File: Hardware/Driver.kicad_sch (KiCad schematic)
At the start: 6 parts, among them Q1 MOSFET_CONTACTOR, Q2 MOSFET_PRECHARGE

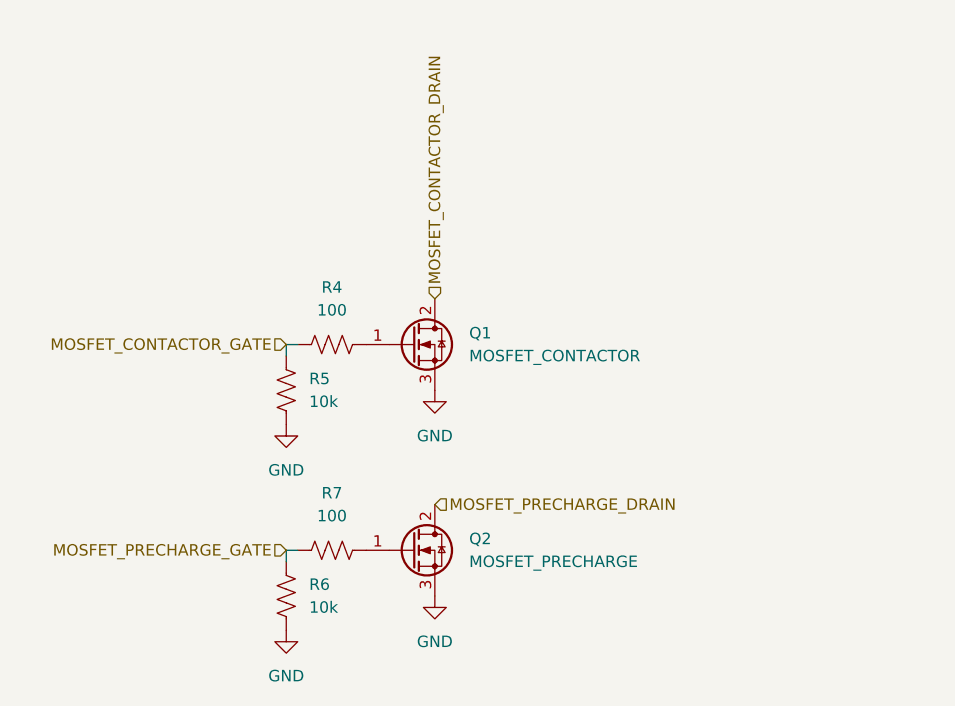
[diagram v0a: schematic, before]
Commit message: Restructure VCU schema
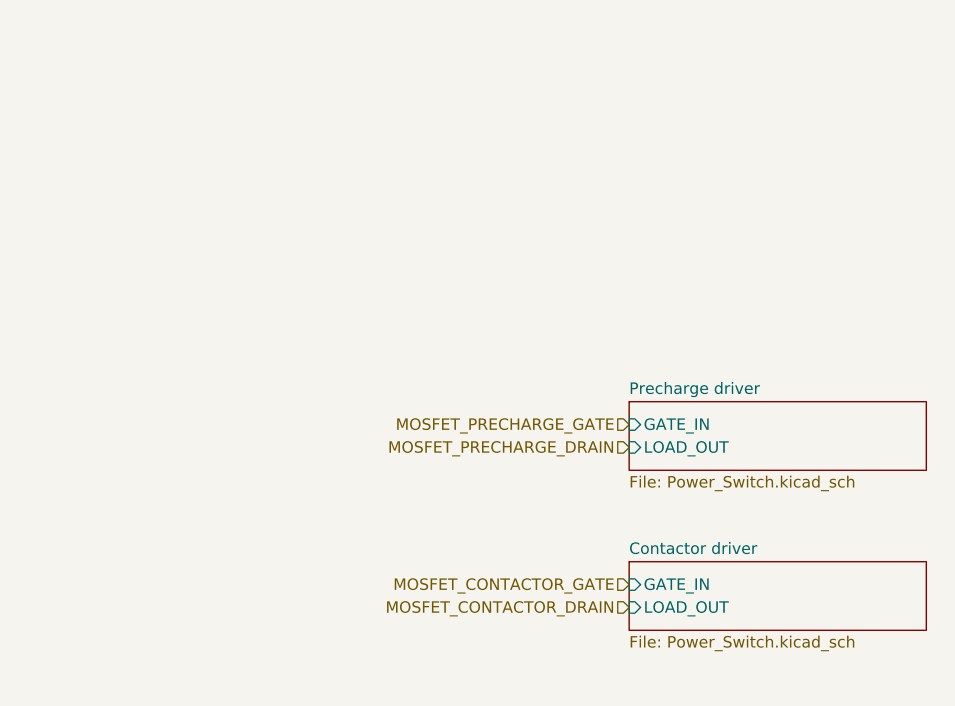
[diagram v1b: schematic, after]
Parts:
- removed Q1: MOSFET_CONTACTOR, Package_QFP:TQFP-44_10x10mm_P0.8mm, symbol Transistor_FET:Q_NMOS_GDS
- removed Q2: MOSFET_PRECHARGE, Package_QFP:TQFP-44_10x10mm_P0.8mm, symbol Transistor_FET:Q_NMOS_GDS
- removed R4, R7: 100, Package_DFN_QFN:WDFN-10-1EP_3x3mm_P0.5mm_EP1.8x2.5mm, symbol Device:R_US
- removed R5, R6: 10k, Package_DFN_QFN:WDFN-10-1EP_3x3mm_P0.5mm_EP1.8x2.5mm, symbol Device:R_US
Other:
- added sheet Contactor driver (Power_Switch.kicad_sch)
- added sheet Precharge driver (Power_Switch.kicad_sch)
